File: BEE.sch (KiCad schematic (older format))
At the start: 44 parts, among them J1 RPI1_header, J10 Conn_01x02, J11 Conn_01x02, J12 Conn_01x02, J13 Conn_01x06, J14 Conn_01x03, J15 Conn_01x03, J16 Conn_01x08, J17 Conn_01x03, J2 Conn_02x05_Odd_Even, J3 Conn_02x03_Odd_Even, J4 Conn_01x06, J5 Conn_02x10_Odd_Even, J8 Conn_01x08, J9 Conn_01x02, SW1 SW_Push, SW2 SW_Push, SW3 SW_Push, U1 MCP3008, U2 MCP4911

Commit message: revision of fab layer. Ref designator in fab layer. bom
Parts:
- J2: Distributor PN 649-67997-410HLF -> 649-67997-210HLF; Distributor link https://www.mouser.es/ProductDetail/Amphenol-FCI/67997-410H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 -> https://www.mouser.es/ProductDetail/Amphenol-FCI/67997-210H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; Manufacturer PN 67997-410HLF -> 67997-210HLF
- J3: Distributor PN 649-68602-406HLF -> 538-87914-0616; Distributor link https://www.mouser.es/ProductDetail/Amphenol-FCI/68602-406H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 -> https://www.mouser.es/ProductDetail/Molex/87914-0616?qs=sGA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; Manufacturer Amphenol FCI -> Molex; Manufacturer PN 68602-406HLF -> 87914-0616
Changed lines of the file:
@@
 F 3 "https://www.mouser.es/datasheet/2/18/67996-1142923.pdf" H 8850 3450 50  0001 C CNN
 F 4 "Mouser" H 0   50  50  0001 C CNN "Distributor"
-F 5 "649-67997-410HLF " H 0   50  50  0001 C CNN "Distributor PN"
-F 6 "https://www.mouser.es/ProductDetail/Amphenol-FCI/67997-410HLF?qs=sGAEpiMZZMs%252BGHln7q6pmxAVkKtOEC39%252BPx3y%2Fg6zsA%3D" H 0   50  50  0001 C CNN "Distributor link"
+F 5 "649-67997-210HLF " H 0   50  50  0001 C CNN "Distributor PN"
+F 6 "https://www.mouser.es/ProductDetail/Amphenol-FCI/67997-210HLF?qs=sGAEpiMZZMs%252BGHln7q6pm2nKUjHUi6l6aE2JnujhSfI%3D" H 0   50  50  0001 C CNN "Distributor link"
 F 7 "Amphenol FCI" H 0   50  50  0001 C CNN "Manufacturer"
-F 8 "67997-410HLF" H 0   50  50  0001 C CNN "Manufacturer PN"
+F 8 "67997-210HLF " H 0   50  50  0001 C CNN "Manufacturer PN"
 	1    8850 3450
 	1    0    0    -1
@@
 F 1 "Conn_02x03_Odd_Even" H 5650 2800 50  0000 C CNN
 F 2 "Connector_PinHeader_2.54mm:PinHeader_2x03_P2.54mm_Vertical" H 5700 3000 50  0001 C CNN
-F 3 "https://www.mouser.es/datasheet/2/18/67996-1142923.pdf" H 5700 3000 50  0001 C CNN
+F 3 "https://www.mouser.es/datasheet/2/276/0879140804_PCB_HEADERS-1091753.pdf" H 5700 3000 50  0001 C CNN
 F 4 "Mouser" H -300 -1400 50  0001 C CNN "Distributor"
-F 5 "649-68602-406HLF " H -300 -1400 50  0001 C CNN "Distributor PN"
-F 6 "https://www.mouser.es/ProductDetail/Amphenol-FCI/68602-406HLF?qs=sGAEpiMZZMs%252BGHln7q6pm2nKUjHUi6l6Whc8wbDWWS8%3D" H -300 -1400 50  0001 C CNN "Distributor link"
-F 7 "Amphenol FCI" H -300 -1400 50  0001 C CNN "Manufacturer"
-F 8 "68602-406HLF" H -300 -1400 50  0001 C CNN "Manufacturer PN"
+F 5 "538-87914-0616 " H -300 -1400 50  0001 C CNN "Distributor PN"
+F 6 "https://www.mouser.es/ProductDetail/Molex/87914-0616?qs=sGAEpiMZZMs%252BGHln7q6pm8NDWwBzqQCNb%2F5NslhjlCw%3D" H -300 -1400 50  0001 C CNN "Distributor link"
+F 7 "Molex" H -300 -1400 50  0001 C CNN "Manufacturer"
+F 8 "87914-0616" H -300 -1400 50  0001 C CNN "Manufacturer PN"
 	1    5700 3000
 	1    0    0    -1

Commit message: mounting holes 2.7mm
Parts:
- H1, H2, H3, H4: footprint MountingHole:MountingHole_2.5mm -> MountingHole:MountingHole_2.7mm_M2.5
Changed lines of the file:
@@
 F 0 "H1" H 950 5950 50  0000 L CNN
 F 1 "MountingHole" H 650 5850 50  0000 L CNN
-F 2 "MountingHole:MountingHole_2.5mm" H 850 5950 50  0001 C CNN
+F 2 "MountingHole:MountingHole_2.7mm_M2.5" H 850 5950 50  0001 C CNN
 F 3 "~" H 850 5950 50  0001 C CNN
 	1    850  5950
@@
 F 0 "H2" H 950 6200 50  0000 L CNN
 F 1 "MountingHole" H 650 6100 50  0000 L CNN
-F 2 "MountingHole:MountingHole_2.5mm" H 850 6200 50  0001 C CNN
+F 2 "MountingHole:MountingHole_2.7mm_M2.5" H 850 6200 50  0001 C CNN
 F 3 "~" H 850 6200 50  0001 C CNN
 	1    850  6200
@@
 F 0 "H4" H 1450 6200 50  0000 L CNN
 F 1 "MountingHole" H 1200 6100 50  0000 L CNN
-F 2 "MountingHole:MountingHole_2.5mm" H 1350 6200 50  0001 C CNN
+F 2 "MountingHole:MountingHole_2.7mm_M2.5" H 1350 6200 50  0001 C CNN
 F 3 "~" H 1350 6200 50  0001 C CNN
 	1    1350 6200
@@
 F 0 "H3" H 1450 5950 50  0000 L CNN
 F 1 "MountingHole" H 1150 5850 50  0000 L CNN
-F 2 "MountingHole:MountingHole_2.5mm" H 1350 5950 50  0001 C CNN
+F 2 "MountingHole:MountingHole_2.7mm_M2.5" H 1350 5950 50  0001 C CNN
 F 3 "~" H 1350 5950 50  0001 C CNN
 	1    1350 5950

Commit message: changing some minor things after first prototype test
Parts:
- J1: Distributor PN 649-68691-440HLF -> 571-7-146254-0; Distributor link https://www.mouser.es/ProductDetail/Amphenol-FCI/68691-440H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 -> https://www.mouser.es/ProductDetail/TE-Connectivity-AMP/7-1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; Manufacturer Amphenol FCI -> TE Connectivity / AMP; Manufacturer PN 68691-440HLF -> 7-146254-0
- J10, J11, J12, J9: Distributor PN 571-6404562 -> 649-68001-402HLF; Distributor link https://www.mouser.es/ProductDetail/TE-Connectivity-AMP/640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 -> https://www.mouser.es/ProductDetail/Amphenol-FCI/68001-402H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; Manufacturer TE Connectivity / AMP -> Amphenol FCI; Manufacturer PN 640456-2 -> 68001-402HLF
- J14, J15, J17: Distributor PN 571-6404563 -> 649-68001-403HLF; Distributor link https://www.mouser.es/ProductDetail/TE-Connectivity-AMP/640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 -> https://www.mouser.es/ProductDetail/Amphenol-FCI/68001-403H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; Manufacturer TE Connectivity / AMP -> Amphenol FCI; Manufacturer PN 640456-3 -> 68001-403HLF
- J16, J8: Distributor PN 571-6404568 -> 649-68000-408HLF; Distributor link https://www.mouser.es/ProductDetail/TE-Connectivity-AMP/640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 -> https://www.mouser.es/ProductDetail/Amphenol-FCI/68000-408H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; Manufacturer TE Connectivity / AMP -> Amphenol FCI; Manufacturer PN 640456-8 -> 68000-408HLF
- J5: Distributor PN 649-68691-420HLF -> 649-77313-418-20LF; Distributor link https://www.mouser.es/ProductDetail/Amphenol-FCI/68691-420H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 -> https://www.mouser.es/ProductDetail/Amphenol-FCI/77313-418-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; Manufacturer Amphenol FCI -> Amphenol FCI; Manufacturer PN 68691-420HLF -> 77313-418-20LF
- renumbered D3 to D1, D1 to D3, R3 to R1, R1 to R3
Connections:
- net BCM12_PWM0: now also J3.6 (Pin_6); no longer J3.3 (Pin_3)
- net SW1: now also R4.2, SW1.1; no longer R6.2, SW3.1
- net SW3: now also R6.2, SW3.1; no longer R4.2, SW1.1
- net at BZ1.2 (+): now also J3.3 (Pin_3); no longer J3.6 (Pin_6)
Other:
- moved on the sheet: BZ1

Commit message: wip Resistors and new pin connectors
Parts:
- removed J8: Conn_01x08, Connector_PinHeader_2.54mm:PinHeader_1x08_P2.54mm_Vertical, symbol Connector_Generic:Conn_01x08
- added J18: Conn_01x03, Connector_PinHeader_2.54mm:PinHeader_1x03_P2.54mm_Vertical, symbol Connector_Generic:Conn_01x03
- added J19, J7: Conn_01x08, Connector_PinSocket_2.54mm:PinSocket_1x08_P2.54mm_Vertical, symbol Connector_Generic:Conn_01x08
- added J8: Conn_02x08_Top_Bottom, Connector_PinHeader_2.54mm:PinHeader_2x08_P2.54mm_Vertical, symbol Connector_Generic:Conn_02x08_Odd_Even
- added R10, R14: 15k, Resistor_SMD:R_0805_2012Metric_Pad1.15x1.40mm_HandSolder, symbol Device:R
- added R11, R15: 47k, Resistor_SMD:R_0805_2012Metric_Pad1.15x1.40mm_HandSolder, symbol Device:R
- added R12, R8: 220, Resistor_SMD:R_0805_2012Metric_Pad1.15x1.40mm_HandSolder, symbol Device:R
- added R13, R9: 10k, Resistor_SMD:R_0805_2012Metric_Pad1.15x1.40mm_HandSolder, symbol Device:R
- R4, R5, R6: value 10K -> 10k; Distributor PN 71-CRCW080510K0FKEAC -> 71-CRCW080510K0FKEAC; Manufacturer PN CRCW080510K0FKEAC -> CRCW080510K0FKEAC
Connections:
- net +3V3: now also J18.1 (Pin_1)
- net +5V: now also J18.3 (Pin_3)
- net GND: now also R10.2, R11.2, R12.2, R13.2, R14.2, R15.2, R8.2, R9.2
- net VDD: now also J11.1 (Pin_1); no longer J11.2 (Pin_2)
- net at U1.1 (CH0): now also J8.2 (Pin_2)
- net at U1.15 (Vref): now also J11.2 (Pin_2); no longer J11.1 (Pin_1)
- net at U1.2 (CH1): now also J8.4 (Pin_4)
- net at U1.3 (CH2): now also J8.6 (Pin_6)
- net at U1.4 (CH3): now also J8.8 (Pin_8)
- net at U1.5 (CH4): now also J8.10 (Pin_10)
- net at U1.6 (CH5): now also J8.12 (Pin_12)
- net at U1.7 (CH6): now also J8.14 (Pin_14)
- net at U1.8 (CH7): now also J8.16 (Pin_16)
- new net AR0: J7.1 (Pin_1), J8.1 (Pin_1), R12.1
- new net AR1: J7.2 (Pin_2), J8.3 (Pin_3), R8.1
- new net AR2: J7.3 (Pin_3), J8.5 (Pin_5), R13.1
- new net AR3: J7.4 (Pin_4), J8.7 (Pin_7), R9.1
- new net AR4: J7.5 (Pin_5), J8.9 (Pin_9), R14.1
- new net AR5: J7.6 (Pin_6), J8.11 (Pin_11), R10.1
- new net AR6: J7.7 (Pin_7), J8.13 (Pin_13), R15.1
- new net AR7: J7.8 (Pin_8), J8.15 (Pin_15), R11.1
- new net VCC: J18.2 (Pin_2), J19.1 (Pin_1), J19.2 (Pin_2), J19.3 (Pin_3), J19.4 (Pin_4), J19.5 (Pin_5), J19.6 (Pin_6), J19.7 (Pin_7), J19.8 (Pin_8)
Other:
- note added: "Socket"
- moved on the sheet: J11, J15

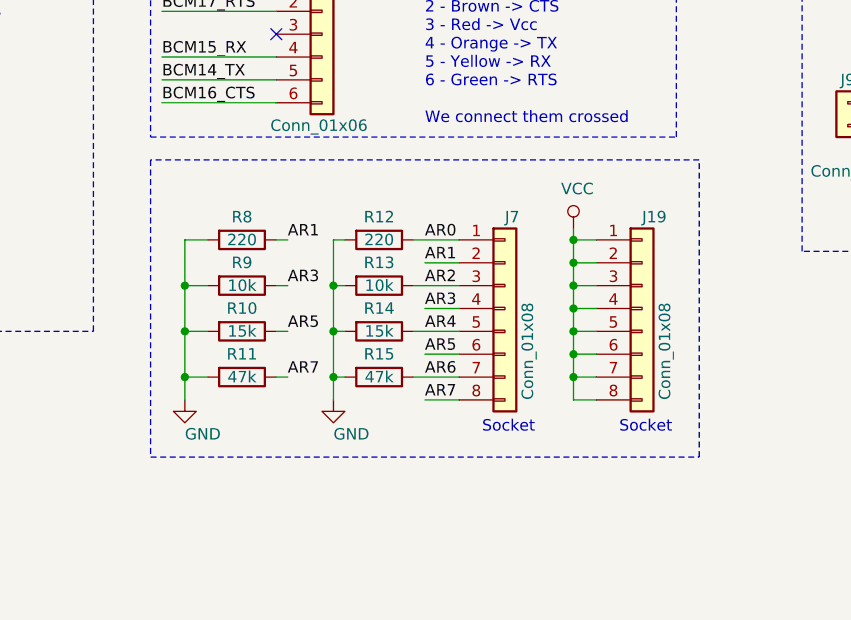
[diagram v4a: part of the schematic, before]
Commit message: vcc down with double socket for external sensors
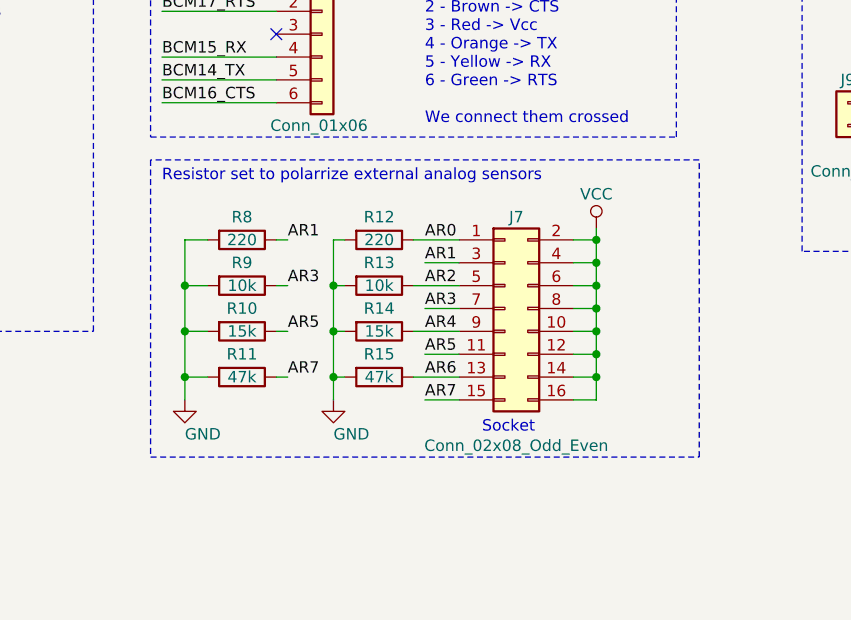
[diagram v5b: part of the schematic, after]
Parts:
- removed J19, J7: Conn_01x08, Connector_PinSocket_2.54mm:PinSocket_1x08_P2.54mm_Vertical, symbol Connector_Generic:Conn_01x08
- added J7: Conn_02x08_Odd_Even, Connector_PinSocket_2.54mm:PinSocket_2x08_P2.54mm_Vertical, symbol Connector_Generic:Conn_02x08_Odd_Even
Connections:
- net AR0: now also J7.1 (Pin_1)
- net AR1: now also J7.3 (Pin_3)
- net AR2: now also J7.5 (Pin_5)
- net AR3: now also J7.7 (Pin_7)
- net AR4: now also J7.9 (Pin_9)
- net AR5: now also J7.11 (Pin_11)
- net AR6: now also J7.13 (Pin_13)
- net AR7: now also J7.15 (Pin_15)
- net VCC: now also J7.10 (Pin_10), J7.12 (Pin_12), J7.14 (Pin_14), J7.16 (Pin_16), J7.2 (Pin_2), J7.4 (Pin_4), J7.6 (Pin_6), J7.8 (Pin_8)
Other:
- note added: "Resistor set to polarrize external analog sensors"
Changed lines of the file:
@@
 	7150 2650 7150 3350
-$Comp
-L Connector_Generic:Conn_01x08 J7
-U 1 1 5E21A26F
-P 5950 5550
-F 0 "J7" H 5950 5950 50  0000 L CNN
-F 1 "Conn_01x08" V 6050 5150 50  0000 L CNN
-F 2 "Connector_PinSocket_2.54mm:PinSocket_1x08_P2.54mm_Vertical" H 5950 5550 50  0001 C CNN
-F 3 "" H 5950 5550 50  0001 C CNN
-F 4 "Mouser" H -3650 3900 50  0001 C CNN "Distributor"
-F 5 " 992-8FX1L-254MM " H -3650 3900 50  0001 C CNN "Distributor PN"
-F 6 "https://www.mouser.es/ProductDetail/Gravitech/8Fx1L-254mm?qs=sGAEpiMZZMs%252BGHln7q6pmy2YKQ02S1gmaSYieH0svFDvlY3s6aL18w%3D%3D" H -3650 3900 50  0001 C CNN "Distributor link"
-F 7 "Gravitech " H -3650 3900 50  0001 C CNN "Manufacturer"
-F 8 "8Fx1L-254mm" H -3650 3900 50  0001 C CNN "Manufacturer PN"
-	1    5950 5550
-	1    0    0    -1
-$EndComp
 $Comp
 L Device:R R12
@@
 L power:VCC #PWR036
 U 1 1 5EB6A4FD
-P 6250 5200
-F 0 "#PWR036" H 6250 5050 50  0001 C CNN
-F 1 "VCC" H 6267 5373 50  0000 C CNN
-F 2 "" H 6250 5200 50  0001 C CNN
-F 3 "" H 6250 5200 50  0001 C CNN
-	1    6250 5200
-	1    0    0    -1
-$EndComp
-Wire Wire Line
-	6250 5200 6250 5250
-Wire Wire Line
-	6250 5250 6350 5250
-Wire Wire Line
-	6250 5250 6250 5350
-Wire Wire Line
-	6250 5950 6350 5950
-Connection ~ 6250 5250
-Wire Wire Line
-	6350 5850 6250 5850
-Connection ~ 6250 5850
-Wire Wire Line
-	6250 5850 6250 5950
-Wire Wire Line
-	6350 5750 6250 5750
-Connection ~ 6250 5750
-Wire Wire Line
-	6250 5750 6250 5850
-Wire Wire Line
-	6350 5650 6250 5650
-Connection ~ 6250 5650
-Wire Wire Line
-	6250 5650 6250 5750
-Wire Wire Line
-	6350 5550 6250 5550
-Connection ~ 6250 5550
-Wire Wire Line
-	6250 5550 6250 5650
-Wire Wire Line
-	6350 5450 6250 5450
-Connection ~ 6250 5450
-Wire Wire Line
-	6250 5450 6250 5550
-Wire Wire Line
-	6350 5350 6250 5350
-Connection ~ 6250 5350
-Wire Wire Line
-	6250 5350 6250 5450
-$Comp
-L Connector_Generic:Conn_01x08 J19
-U 1 1 5EBF8BBB
-P 6550 5550
-F 0 "J19" H 6550 5950 50  0000 L CNN
-F 1 "Conn_01x08" V 6650 5150 50  0000 L CNN
-F 2 "Connector_PinSocket_2.54mm:PinSocket_1x08_P2.54mm_Vertical" H 6550 5550 50  0001 C CNN
-F 3 "" H 6550 5550 50  0001 C CNN
-F 4 "Mouser" H -3050 3900 50  0001 C CNN "Distributor"
-F 5 " 992-8FX1L-254MM " H -3050 3900 50  0001 C CNN "Distributor PN"
-F 6 "https://www.mouser.es/ProductDetail/Gravitech/8Fx1L-254mm?qs=sGAEpiMZZMs%252BGHln7q6pmy2YKQ02S1gmaSYieH0svFDvlY3s6aL18w%3D%3D" H -3050 3900 50  0001 C CNN "Distributor link"
-F 7 "Gravitech " H -3050 3900 50  0001 C CNN "Manufacturer"
-F 8 "8Fx1L-254mm" H -3050 3900 50  0001 C CNN "Manufacturer PN"
-	1    6550 5550
-	1    0    0    -1
-$EndComp
+P 6350 5200
+F 0 "#PWR036" H 6350 5050 50  0001 C CNN
+F 1 "VCC" H 6350 5350 50  0000 C CNN
+F 2 "" H 6350 5200 50  0001 C CNN
+F 3 "" H 6350 5200 50  0001 C CNN
+	1    6350 5200
+	-1   0    0    -1
+$EndComp
+Wire Wire Line
+	6350 5200 6350 5250
+Wire Wire Line
+	6350 5250 6250 5250
+Wire Wire Line
+	6350 5250 6350 5350
+Wire Wire Line
+	6350 5950 6250 5950
+Connection ~ 6350 5250
+Wire Wire Line
+	6250 5850 6350 5850
+Connection ~ 6350 5850
+Wire Wire Line
+	6350 5850 6350 5950
+Wire Wire Line
+	6250 5750 6350 5750
+Connection ~ 6350 5750
+Wire Wire Line
+	6350 5750 6350 5850
+Wire Wire Line
+	6250 5650 6350 5650
+Connection ~ 6350 5650
+Wire Wire Line
+	6350 5650 6350 5750
+Wire Wire Line
+	6250 5550 6350 5550
+Connection ~ 6350 5550
+Wire Wire Line
+	6350 5550 6350 5650
+Wire Wire Line
+	6250 5450 6350 5450
+Connection ~ 6350 5450
+Wire Wire Line
+	6350 5450 6350 5550
+Wire Wire Line
+	6250 5350 6350 5350
+Connection ~ 6350 5350
+Wire Wire Line
+	6350 5350 6350 5450
 Text Notes 5850 6100 0    50   ~ 0
-Socket
-Text Notes 6450 6100 0    50   ~ 0
 Socket
 Wire Wire Line
@@
 Wire Wire Line
 	9250 2050 9400 2050
+$Comp
+L Connector_Generic:Conn_02x08_Odd_Even J7
+U 1 1 5E23FBF6
+P 5950 5550
+F 0 "J7" H 6000 5950 50  0000 C CNN
+F 1 "Conn_02x08_Odd_Even" H 6000 4950 50  0000 C CNN
+F 2 "Connector_PinSocket_2.54mm:PinSocket_2x08_P2.54mm_Vertical" H 5950 5550 50  0001 C CNN
+F 3 "https://www.mouser.es/datasheet/2/276/0901512116_PCB_RECEPTACLES-230157.pdf" H 5950 5550 50  0001 C CNN
+F 4 "Mouser" H 0   0   50  0001 C CNN "Distributor"
+F 5 "Molex" H 0   0   50  0001 C CNN "Manufacturer"
+F 6 " 538-90151-2116 " H 0   0   50  0001 C CNN "Distributor PN"
+F 7 "https://www.mouser.es/ProductDetail/Molex/90151-2116?qs=sGAEpiMZZMs%252BGHln7q6pm%252BS0pk2Wo0Xx4UQ7yBUQDzo%3D" H 0   0   50  0001 C CNN "Distributor link"
+F 8 "90151-2116 " H 0   0   50  0001 C CNN "Manufacturer PN"
+	1    5950 5550
+	1    0    0    -1
+$EndComp
+Text Notes 4450 5000 0    50   ~ 0
+Resistor set to polarrize external analog sensors
 $EndSCHEMATC

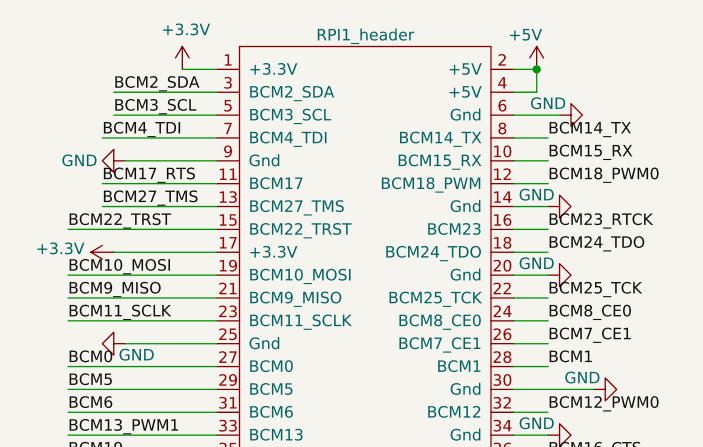
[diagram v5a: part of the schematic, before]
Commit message: replace and reroute: jtag signals on the sides
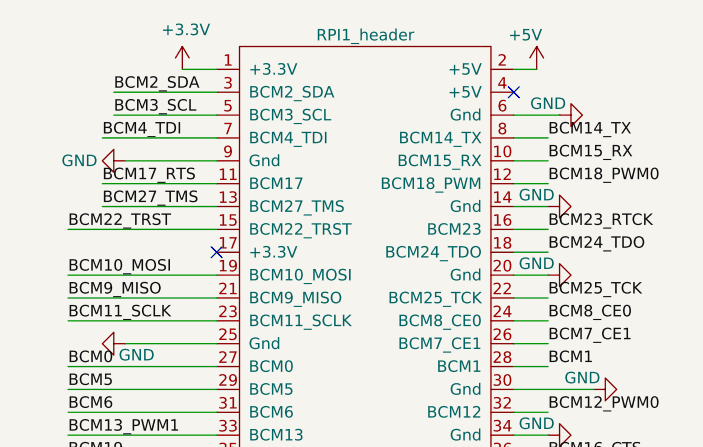
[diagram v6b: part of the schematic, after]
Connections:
- net +3V3: no longer J1.17 (+3.3V)
- net +5V: no longer J1.4 (+5V)
- no-connect marks 4 -> 6
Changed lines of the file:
@@
 	1    0    0    -1
 $EndComp
-Wire Wire Line
-	2800 1050 2900 1050
-Wire Wire Line
-	2900 1050 2900 950
 $Comp
 L power:PWR_FLAG #FLG08
@@
 Wire Wire Line
 	5400 2300 5400 2250
-$Comp
-L power:+3.3V #PWR01
-U 1 1 5E40233B
-P 1050 1750
-F 0 "#PWR01" H 1050 1600 50  0001 C CNN
-F 1 "+3.3V" V 1065 1878 50  0000 L CNN
-F 2 "" H 1050 1750 50  0001 C CNN
-F 3 "" H 1050 1750 50  0001 C CNN
-	1    1050 1750
-	0    -1   -1   0
-$EndComp
-Wire Wire Line
-	1050 1750 1500 1750
 $Comp
 L power:PWR_FLAG #FLG05
@@
 Wire Wire Line
 	2800 1150 3000 1150
-Connection ~ 2900 950
 $Comp
 L power:+3.3V #PWR0101
@@
 Text Notes 4450 5000 0    50   ~ 0
 Resistor set to polarrize external analog sensors
+NoConn ~ 1500 1750
+NoConn ~ 2800 1050
 $EndSCHEMATC
